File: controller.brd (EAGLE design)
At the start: 22 x 22 mm, 5 parts

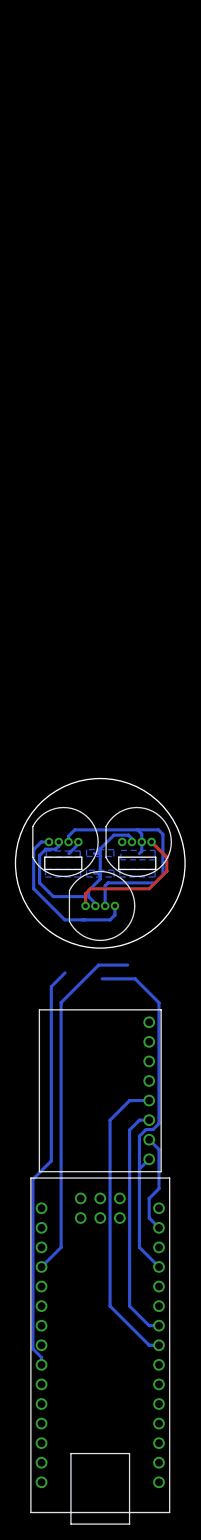
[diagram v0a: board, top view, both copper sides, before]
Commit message: fixed design based on prototype 0
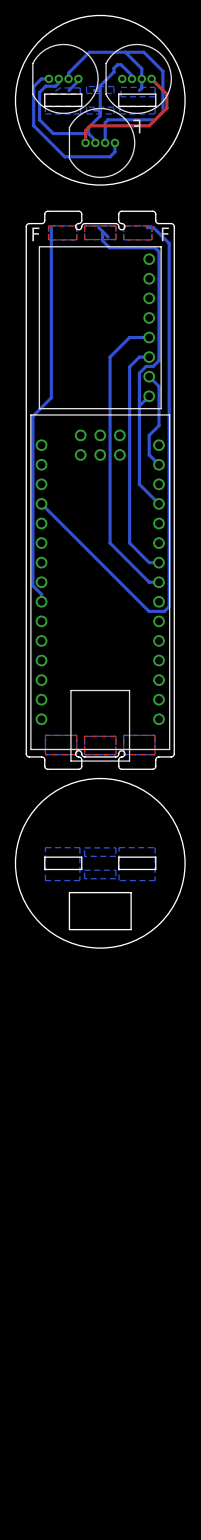
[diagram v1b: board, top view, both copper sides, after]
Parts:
- moved U$1 99.0 mm to (0.00, 36.5)
- moved U$2 99.0 mm to (-4.75, 101.8)
- moved U$3 99.0 mm to (0.00, 93.5)
- moved U$4 99.0 mm to (4.75, 101.8)
- moved U$5 99.0 mm to (0.00, 69.5)
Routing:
- net N$7: track 79.0 -> 110.5 mm
- net N$5: track 55.0 -> 51.9 mm
- net N$1: track 77.5 -> 79.2 mm
- added copper zone on layer 16, net N$11
- added copper zone on layer 16, net N$12
- added copper zone on layer 16, net N$13
- added copper zone on layer 16, net N$14
- added copper zone on layer 16, net N$15
- added copper zone on layer 16, net N$16
- added copper zone on layer 1, net N$17
- added copper zone on layer 1, net N$18
- added copper zone on layer 1, net N$19
- added copper zone on layer 1, net N$20
- added copper zone on layer 1, net N$21
- added copper zone on layer 1, net N$22
- added copper zone on layer 16, net N$23
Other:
- board size 22 x 22 mm -> 22 x 121 mm
- board text added: "B"
- board text added: "F"
